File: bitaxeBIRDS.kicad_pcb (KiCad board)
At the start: 6 copper layers, 65 x 112 mm, 203 parts, among them J1001 XT30, J3001 Conn_01x04, J5001 Conn_01x04, J6 USB_C_Receptacle_USB2.0, SW1 SWITCH-SPST, SW2 SWITCH-SPST, U2001 TPSM861253RDXR, U2003 TPS546D24S, U2004 TPS546D24S, U27 RP2040, U3 TPS22919DCKR, U4001 MCP1824T-1202E/OT, U4002 25MHz, U4003 BM1370_mode1, U4004 MCP1824T-0802E, U4005 SN74AVC4T774, U4006 BM1370_mode1, U5001 EMC2103-2, U8 W25Q16JVUXIQ TR, U9 SK6812, Y1 12MHz

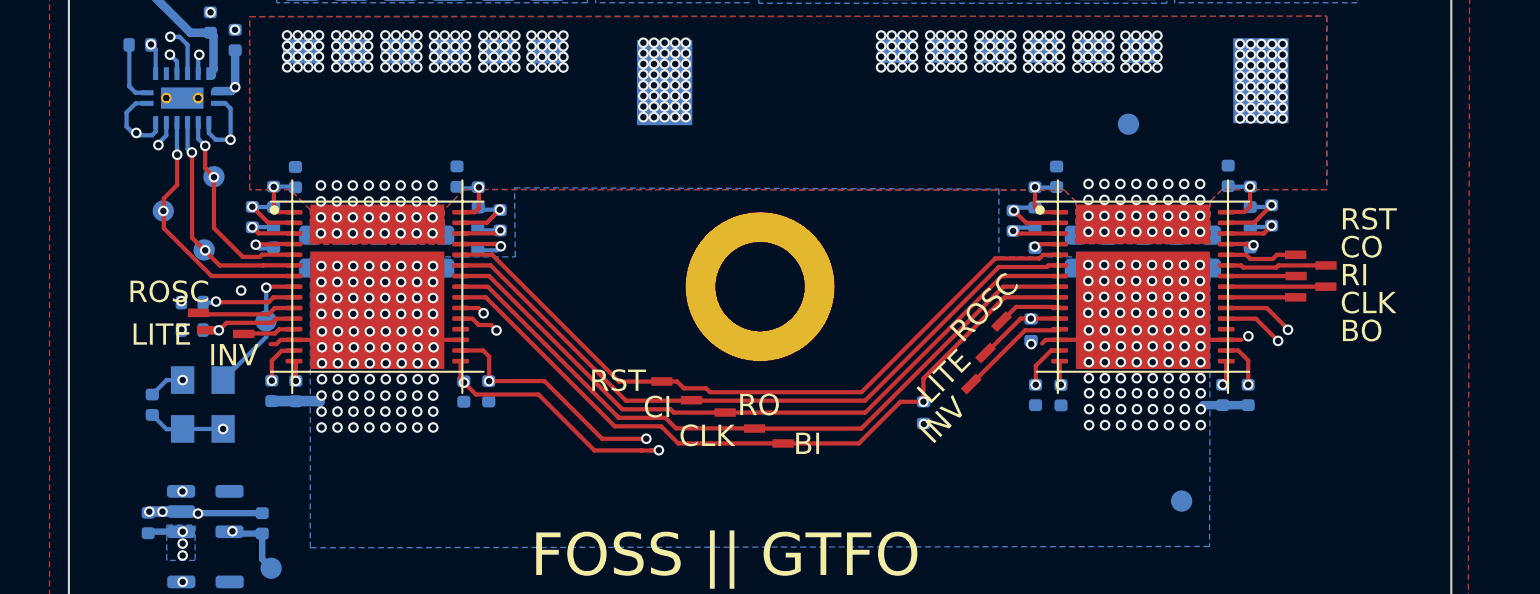
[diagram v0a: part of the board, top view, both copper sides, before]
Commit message: started to piece in the BZM2 into schematic
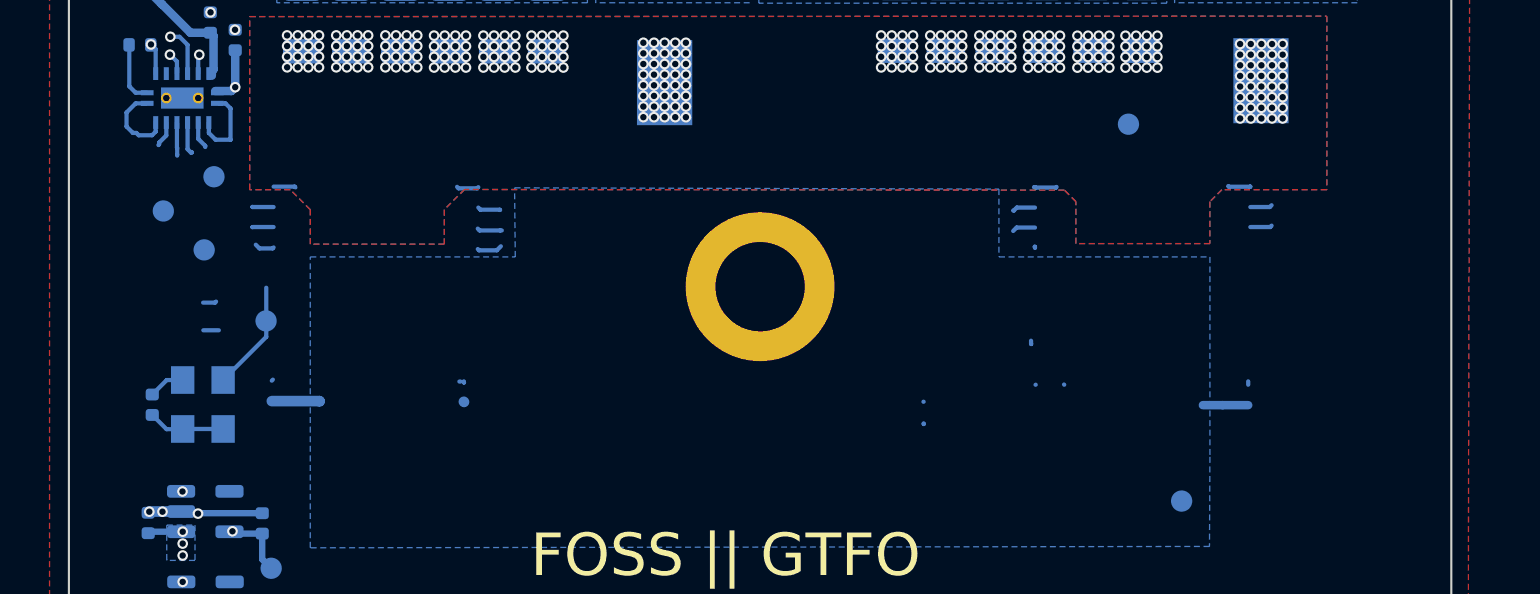
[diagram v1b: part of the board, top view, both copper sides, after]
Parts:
- removed C4002, C4003, C4004, C4005, C4006, C4008, C4012, C4013, C4015, C4016, C4018, C4020, C4023, C4025, C4026, C4027, C4028, C4029, C4031, C4033, C4034, C4036, C4038, C4040: 1uF, Capacitor_SMD:C_0402_1005Metric
- removed C4010, C4014, C4017, C4019, C4022, C4030, C4032, C4035, C4039, C4041: 10uF, Capacitor_SMD:C_0603_1608Metric
- removed R4001: 10k, Resistor_SMD:R_0402_1005Metric
- removed R4002, R4004: 1k, Resistor_SMD:R_0402_1005Metric
- removed R4003: 2k, Resistor_SMD:R_0402_1005Metric
- removed TP4001, TP4007: ROSC, bitaxe:TestPoint_Pad_1.0x0.4mm
- removed TP4002, TP4008: LITE, bitaxe:TestPoint_Pad_1.0x0.4mm
- removed TP4003, TP4017: INV, bitaxe:TestPoint_Pad_1.0x0.4mm
- removed TP4009, TP4021: RST, bitaxe:TestPoint_Pad_1.0x0.4mm
- removed TP4010: CI, bitaxe:TestPoint_Pad_1.0x0.4mm
- removed TP4011: RO, bitaxe:TestPoint_Pad_1.0x0.4mm
- removed TP4012, TP4024: CLK, bitaxe:TestPoint_Pad_1.0x0.4mm
- removed TP4013: BI, bitaxe:TestPoint_Pad_1.0x0.4mm
- removed TP4022: CO, bitaxe:TestPoint_Pad_1.0x0.4mm
- removed TP4023: RI, bitaxe:TestPoint_Pad_1.0x0.4mm
- removed TP4025: BO, bitaxe:TestPoint_Pad_1.0x0.4mm
- removed U4003, U4006: BM1370_mode1, bitaxe:BM1370
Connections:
- C103 pad 2: /Data/3V3 -> /3V3
- C104 pad 2: /Data/3V3 -> /3V3
- C105 pad 2: /Data/3V3 -> /3V3
- C106 pad 2: /Data/3V3 -> /3V3
- C107 pad 2: /Data/3V3 -> /3V3
- C108 pad 2: /Data/3V3 -> /3V3
- C109 pad 2: /Data/3V3 -> /3V3
- C110 pad 2: /Data/3V3 -> /3V3
- C4001 pad 1: GND -> /ASIC/GND
- C4007 pad 1: GND -> /ASIC/GND
- C4009 pad 2: GND -> /ASIC/GND
- C4011 pad 1: GND -> /ASIC/GND
- C4021 pad 1: GND -> /ASIC/GND
- C4024 pad 2: GND -> /ASIC/GND
- C4037 pad 2: GND -> /ASIC/GND
- C99 pad 2: /Data/3V3 -> /3V3
- J3001 pad 2: /Data/3V3 -> /3V3
- R1 pad 2: /Data/3V3 -> /3V3
- R19 pad 1: /Data/3V3 -> /3V3
- R20 pad 2: /Data/3V3 -> /3V3
- R34 pad 2: /Data/3V3 -> /3V3
- R4005 pad 1: GND -> /ASIC/GND
- R50 pad 1: /Data/3V3 -> /3V3
- R5001 pad 2: /ASIC/TEMP2_P -> /fan/TEMP2_P
- R5002 pad 2: /ASIC/TEMP2_N -> /fan/TEMP2_N
- R5003 pad 2: /ASIC/TEMP1_P -> /fan/TEMP1_P
- R5004 pad 2: /ASIC/TEMP1_N -> /fan/TEMP1_N
- U27 pad 1: /Data/3V3 -> /3V3
- U27 pad 10: /Data/3V3 -> /3V3
- U27 pad 22: /Data/3V3 -> /3V3
- U27 pad 33: /Data/3V3 -> /3V3
- U27 pad 42: /Data/3V3 -> /3V3
- U27 pad 43: /Data/3V3 -> /3V3
- U27 pad 44: /Data/3V3 -> /3V3
- U27 pad 48: /Data/3V3 -> /3V3
- U27 pad 49: /Data/3V3 -> /3V3
- U4001 pad 2: GND -> /ASIC/GND
- U4002 pad 2: GND -> /ASIC/GND
- U4004 pad 2: GND -> /ASIC/GND
- U4005 pad 1: GND -> /ASIC/GND
- U4005 pad 10: GND -> /ASIC/GND
- U4005 pad 2: GND -> /ASIC/GND
- U4005 pad 6: GND -> /ASIC/GND
- U8 pad 8: /Data/3V3 -> /3V3
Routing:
- net /ASIC/TEMP2_N: track 54.9 -> 0.00 mm, vias 2 -> 0
- net /ASIC/TEMP2_P: track 51.9 -> 0.00 mm, vias 2 -> 0
- net Net-(U4003-VDD3_1): track 40.5 -> 0.00 mm, vias 2 -> 0
- net Net-(U4003-VDD2_1): track 38.5 -> 0.00 mm, vias 2 -> 0
- net Net-(U4003-VDD1_1): track 37.8 -> 0.00 mm, vias 2 -> 0
- net /fan/TEMP2_N: track 0.00 -> 37.5 mm, vias 0 -> 1
- net GND: track 94.4 -> 57.3 mm, vias 574 -> 376
- net /fan/TEMP2_P: track 0.00 -> 35.7 mm, vias 0 -> 1
- net Net-(U4003-BO): track 34.5 -> 0.00 mm, vias 1 -> 0
- net Net-(U4003-CLKO): track 33.8 -> 0.00 mm
- net /ASIC/1V2: track 103.9 -> 70.3 mm, vias 7 -> 2
- net Net-(U4003-NRSTO): track 33.5 -> 0.00 mm
- net Net-(U4003-RI): track 33.5 -> 0.00 mm
- net Net-(U4003-CO): track 33.4 -> 0.00 mm
- net /ASIC/0V8: track 57.4 -> 24.2 mm, vias 4 -> 1
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
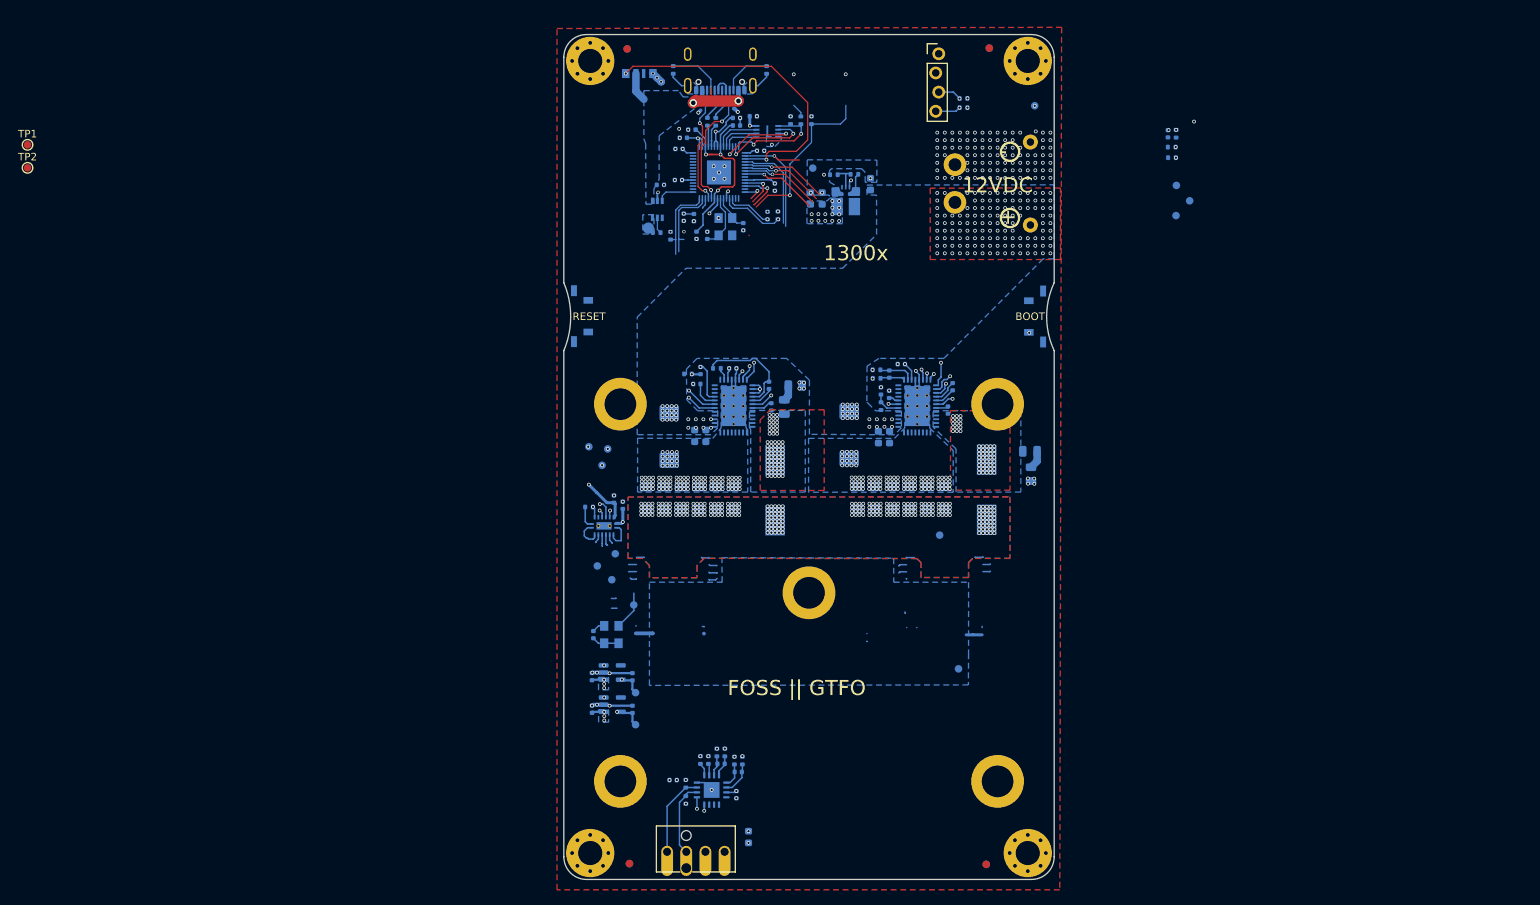
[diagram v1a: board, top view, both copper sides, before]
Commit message: finished adding ASICs to schematic. Change VR to single phase 2.8V output
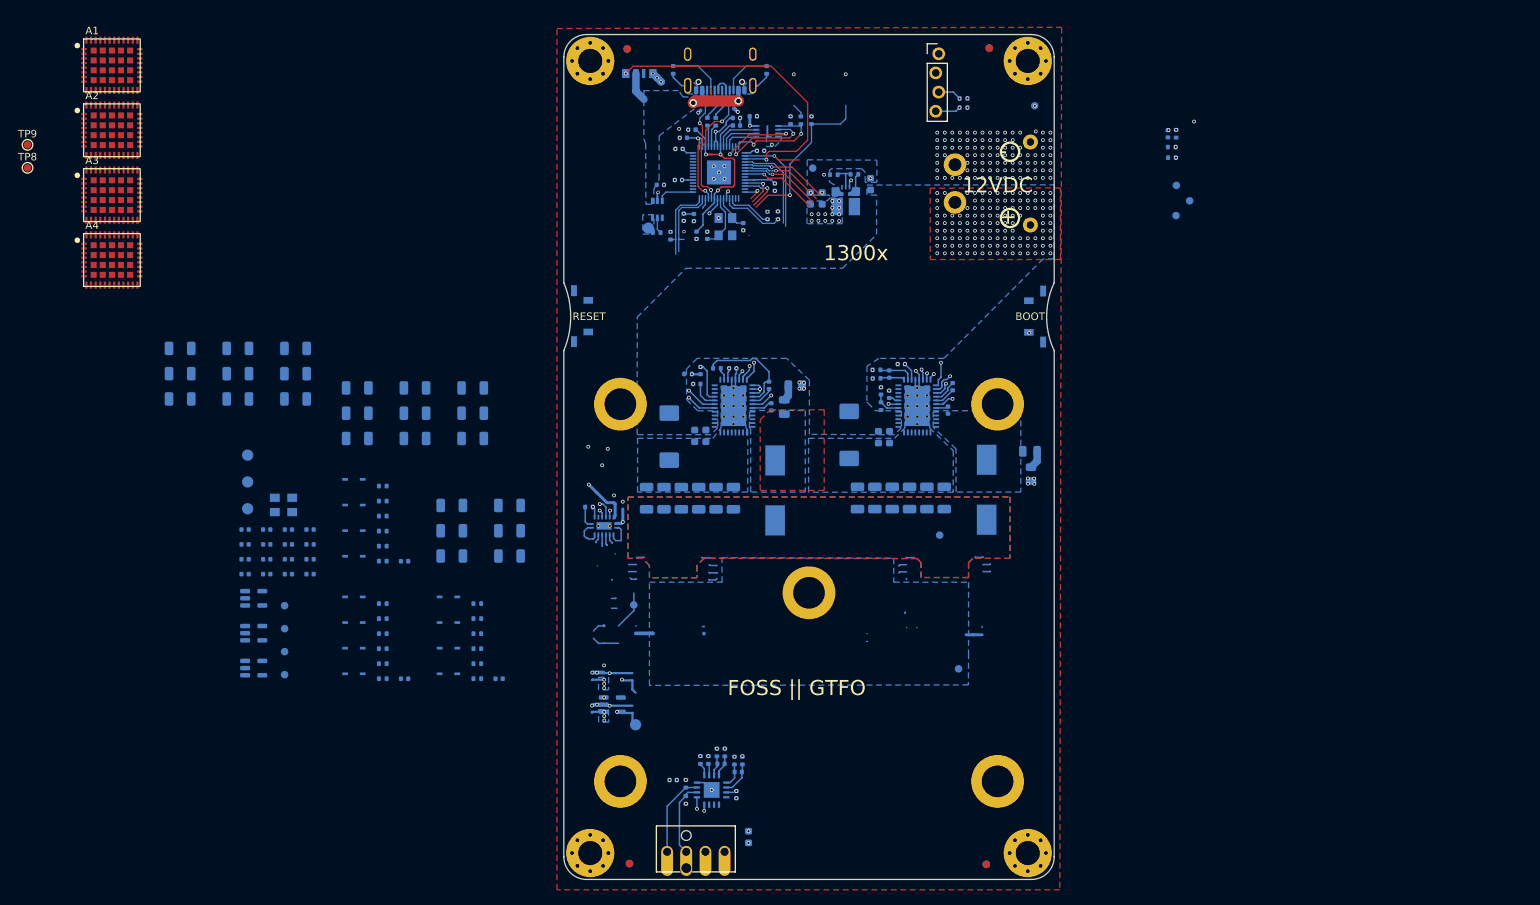
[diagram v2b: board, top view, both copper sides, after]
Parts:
- removed C4001, C4007, C4011, C4021: 1uF, Capacitor_SMD:C_0402_1005Metric
- removed C4009, C4024, C4037: 0.1uF, Capacitor_SMD:C_0402_1005Metric
- removed TP4006: 0V8, bitaxe:TestPoint_Pad_D1.0mm
- removed TP4014, TP4018: RST, bitaxe:TestPoint_Pad_D1.0mm
- removed TP4015, TP4019: TX, bitaxe:TestPoint_Pad_D1.0mm
- removed TP4016, TP4020: RX, bitaxe:TestPoint_Pad_D1.0mm
- removed U4002: 25MHz, bitaxe:SMD3225-4P
- removed U4004: MCP1824T-0802E, Package_TO_SOT_SMD:SOT-23-5
- added A1: BZM2_MODE0, bitaxe:bzm2, F.Cu at (38.6, 42.1)
- added A2: BZM2_MODE1, bitaxe:bzm2, F.Cu at (38.6, 50.7)
- added A3: BZM2_MODE0, bitaxe:bzm2, F.Cu at (38.6, 59.3)
- added A4: BZM2_MODE1, bitaxe:bzm2, F.Cu at (38.6, 67.9)
- added C100: 100uF, Capacitor_SMD:C_1206_3216Metric, B.Cu at (86.4, 88.2)
- added C101: 100uF, Capacitor_SMD:C_1206_3216Metric, B.Cu at (86.4, 84.8)
- added C107: 100uF, Capacitor_SMD:C_1206_3216Metric, B.Cu at (78.8, 91.5)
- added C108: 100uF, Capacitor_SMD:C_1206_3216Metric, B.Cu at (78.8, 88.2)
- added C109: 100uF, Capacitor_SMD:C_1206_3216Metric, B.Cu at (78.8, 84.8)
- added C115: 100uF, Capacitor_SMD:C_1206_3216Metric, B.Cu at (55.3, 86.3)
- added C116: 100uF, Capacitor_SMD:C_1206_3216Metric, B.Cu at (55.3, 83.0)
- added C117: 100uF, Capacitor_SMD:C_1206_3216Metric, B.Cu at (55.3, 79.6)
- added C123: 100uF, Capacitor_SMD:C_1206_3216Metric, B.Cu at (62.9, 86.3)
- added C124: 100uF, Capacitor_SMD:C_1206_3216Metric, B.Cu at (62.9, 83.0)
- added C125: 100uF, Capacitor_SMD:C_1206_3216Metric, B.Cu at (62.9, 79.6)
- added C131: 100uF, Capacitor_SMD:C_1206_3216Metric, B.Cu at (47.6, 86.3)
- added C132: 100uF, Capacitor_SMD:C_1206_3216Metric, B.Cu at (47.6, 83.0)
- added C133: 100uF, Capacitor_SMD:C_1206_3216Metric, B.Cu at (47.6, 79.6)
- added C139: 100uF, Capacitor_SMD:C_1206_3216Metric, B.Cu at (71.1, 91.5)
- added C140: 100uF, Capacitor_SMD:C_1206_3216Metric, B.Cu at (71.1, 88.2)
- added C141: 100uF, Capacitor_SMD:C_1206_3216Metric, B.Cu at (71.1, 84.8)
- added C142: 1000pF, Capacitor_SMD:C_0402_1005Metric, B.Cu at (77.4, 123.4)
- added C143: 1000pF, Capacitor_SMD:C_0402_1005Metric, B.Cu at (77.4, 107.8)
- added C144: 1000pF, Capacitor_SMD:C_0402_1005Metric, B.Cu at (89.9, 123.4)
- added C57: 0.1uF, Capacitor_SMD:C_0402_1005Metric, B.Cu at (56.2, 109.5)
- added C58: 0.1uF, Capacitor_SMD:C_0402_1005Metric, B.Cu at (56.2, 107.6)
- added C59: 0.1uF, Capacitor_SMD:C_0402_1005Metric, B.Cu at (56.2, 105.6)
- added C60: 120pF, Capacitor_SMD:C_0402_1005Metric, B.Cu at (56.2, 103.6)
- added C61: 120pF, Capacitor_SMD:C_0402_1005Metric, B.Cu at (59.1, 109.5)
- added C62: 120pF, Capacitor_SMD:C_0402_1005Metric, B.Cu at (59.1, 107.6)
- added C63: 120pF, Capacitor_SMD:C_0402_1005Metric, B.Cu at (59.1, 105.6)
- added C64: 120pF, Capacitor_SMD:C_0402_1005Metric, B.Cu at (59.1, 103.6)
- added C65: 1uF, Capacitor_SMD:C_0402_1005Metric, B.Cu at (62.0, 109.5)
- added C66: 1uF, Capacitor_SMD:C_0402_1005Metric, B.Cu at (62.0, 107.6)
- added C67: 1uF, Capacitor_SMD:C_0402_1005Metric, B.Cu at (62.0, 105.6)
- added C68: 1uF, Capacitor_SMD:C_0402_1005Metric, B.Cu at (62.0, 103.6)
- added C69: 1uF, Capacitor_SMD:C_0402_1005Metric, B.Cu at (64.9, 109.5)
- added C70: 1uF, Capacitor_SMD:C_0402_1005Metric, B.Cu at (64.9, 107.6)
- added C71: 1uF, Capacitor_SMD:C_0402_1005Metric, B.Cu at (64.9, 105.6)
- added C72: 1uF, Capacitor_SMD:C_0402_1005Metric, B.Cu at (64.9, 103.6)
- added C83: 100uF, Capacitor_SMD:C_1206_3216Metric, B.Cu at (91.3, 107.1)
- added C84: 100uF, Capacitor_SMD:C_1206_3216Metric, B.Cu at (91.3, 103.8)
- added C85: 100uF, Capacitor_SMD:C_1206_3216Metric, B.Cu at (91.3, 100.4)
- added C91: 100uF, Capacitor_SMD:C_1206_3216Metric, B.Cu at (83.7, 107.1)
- added C92: 100uF, Capacitor_SMD:C_1206_3216Metric, B.Cu at (83.7, 103.8)
- added C93: 100uF, Capacitor_SMD:C_1206_3216Metric, B.Cu at (83.7, 100.4)
- added C99: 100uF, Capacitor_SMD:C_1206_3216Metric, B.Cu at (86.4, 91.5)
- added D1: 1SS380VMTE-17, bitaxe:SOD-323FLUMD2_ROM, B.Cu at (70.7, 122.7)
- added D10: 1SS380VMTE-17, bitaxe:SOD-323FLUMD2_ROM, B.Cu at (83.2, 119.3)
- added D11: 1SS380VMTE-17, bitaxe:SOD-323FLUMD2_ROM, B.Cu at (83.2, 115.9)
- added D12: 1SS380VMTE-17, bitaxe:SOD-323FLUMD2_ROM, B.Cu at (83.2, 112.5)
- added D2: 1SS380VMTE-17, bitaxe:SOD-323FLUMD2_ROM, B.Cu at (70.7, 119.3)
- added D3: 1SS380VMTE-17, bitaxe:SOD-323FLUMD2_ROM, B.Cu at (70.7, 115.9)
- added D4: 1SS380VMTE-17, bitaxe:SOD-323FLUMD2_ROM, B.Cu at (70.7, 112.5)
- added D5: 1SS380VMTE-17, bitaxe:SOD-323FLUMD2_ROM, B.Cu at (70.7, 107.2)
- added D6: 1SS380VMTE-17, bitaxe:SOD-323FLUMD2_ROM, B.Cu at (70.7, 103.8)
- added D7: 1SS380VMTE-17, bitaxe:SOD-323FLUMD2_ROM, B.Cu at (70.7, 100.4)
- added D8: 1SS380VMTE-17, bitaxe:SOD-323FLUMD2_ROM, B.Cu at (70.7, 97.0)
- added D9: 1SS380VMTE-17, bitaxe:SOD-323FLUMD2_ROM, B.Cu at (83.2, 122.7)
- added R35: 1k, Resistor_SMD:R_0402_1005Metric, B.Cu at (74.5, 123.4)
- added R36: 1k, Resistor_SMD:R_0402_1005Metric, B.Cu at (74.5, 121.4)
- added R37: 1k, Resistor_SMD:R_0402_1005Metric, B.Cu at (74.5, 119.4)
- added R38: 1k, Resistor_SMD:R_0402_1005Metric, B.Cu at (74.5, 117.4)
- added R39: 1k, Resistor_SMD:R_0402_1005Metric, B.Cu at (74.5, 115.4)
- added R40: 1k, Resistor_SMD:R_0402_1005Metric, B.Cu at (74.5, 113.4)
- added R41: 1k, Resistor_SMD:R_0402_1005Metric, B.Cu at (74.5, 107.8)
- added R42: 1k, Resistor_SMD:R_0402_1005Metric, B.Cu at (74.5, 105.8)
- added R43: 1k, Resistor_SMD:R_0402_1005Metric, B.Cu at (74.5, 103.8)
- added R44: 1k, Resistor_SMD:R_0402_1005Metric, B.Cu at (74.5, 101.8)
- added R45: 1k, Resistor_SMD:R_0402_1005Metric, B.Cu at (74.5, 99.8)
- added R46: 1k, Resistor_SMD:R_0402_1005Metric, B.Cu at (74.5, 97.9)
- added R47: 1k, Resistor_SMD:R_0402_1005Metric, B.Cu at (87.0, 123.4)
- added R48: 1k, Resistor_SMD:R_0402_1005Metric, B.Cu at (87.0, 121.4)
- added R49: 1k, Resistor_SMD:R_0402_1005Metric, B.Cu at (87.0, 119.4)
- added R50: 1k, Resistor_SMD:R_0402_1005Metric, B.Cu at (87.0, 117.4)
- added R51: 1k, Resistor_SMD:R_0402_1005Metric, B.Cu at (87.0, 115.4)
- added R52: 1k, Resistor_SMD:R_0402_1005Metric, B.Cu at (87.0, 113.4)
- added TP11: CLKI, TestPoint:TestPoint_Pad_D1.0mm, B.Cu at (61.5, 122.9)
- added TP12: CLKI, TestPoint:TestPoint_Pad_D1.0mm, B.Cu at (61.5, 119.8)
- added TP13: CLKI, TestPoint:TestPoint_Pad_D1.0mm, B.Cu at (61.5, 116.8)
- added TP14: CLKI, TestPoint:TestPoint_Pad_D1.0mm, B.Cu at (61.5, 113.7)
- added TP15: 1V2-4, TestPoint:TestPoint_Pad_D1.5mm, B.Cu at (56.6, 100.9)
- added TP16: 1V2-3, TestPoint:TestPoint_Pad_D1.5mm, B.Cu at (56.6, 97.3)
- added TP17: 1V2-2, TestPoint:TestPoint_Pad_D1.5mm, B.Cu at (56.6, 93.8)
- added U10: MCP1824T-1202E/OT, Package_TO_SOT_SMD:SOT-23-5, B.Cu at (57.4, 117.4)
- added U11: MCP1824T-1202E/OT, Package_TO_SOT_SMD:SOT-23-5, B.Cu at (57.4, 112.7)
- added U9: MCP1824T-1202E/OT, Package_TO_SOT_SMD:SOT-23-5, B.Cu at (57.4, 122.0)
- added Y2: 50MHz, bitaxe:OSC_ECS-3225MV-500-CN-TR, B.Cu at (61.3, 100.4)
- TP10: renamed from TP4005; footprint bitaxe:TestPoint_Pad_D1.0mm -> TestPoint:TestPoint_Pad_D1.0mm
- TP18: renamed from TP4004; value 1V2 -> 1V2-1; footprint bitaxe:TestPoint_Pad_D1.0mm -> TestPoint:TestPoint_Pad_D1.5mm
- renumbered C2001 to C1, C2012 to C10, C2013 to C11, C2016 to C14, C2017 to C15, C2018 to C16, C2004 to C2, C2023 to C21, C2024 to C22, C2025 to C23, C2026 to C24, C2027 to C25, C2028 to C26, C2029 to C27, C2030 to C28, C2031 to C29, C2005 to C3, C2032 to C30, C2033 to C31, C2034 to C32, C2035 to C33, C2036 to C34, C2037 to C35, C2038 to C36, C2039 to C37, C2040 to C38, C2041 to C39, C2006 to C4, C2042 to C40, C2043 to C41, C96 to C42, C97 to C43, C99 to C44, C26 to C45, C100 to C46, C101 to C47, C102 to C48, C103 to C49, C2007 to C5, C104 to C50, C105 to C51, C106 to C52, C107 to C53, C108 to C54, C109 to C55, C110 to C56, C2008 to C6, C2009 to C7, C5001 to C73, C5002 to C74, C5003 to C75, C5004 to C76, C5005 to C77, C2010 to C8, C2011 to C9, FID1001 to FID1, FID1002 to FID2, FID1003 to FID3, FID1004 to FID4, H1001 to H1, H1002 to H2, H1003 to H3, H1004 to H4, HS1001 to HS1, J1001 to J1, J6 to J2, J3001 to J3, J5001 to J4, L2001 to L1, L2002 to L2, NT2001 to NT1, NT2002 to NT2, R2001 to R1, R2010 to R10, R2011 to R11, R2012 to R12, R2013 to R13, R2014 to R14, R50 to R15, R51 to R16, R52 to R17, R55 to R18, R34 to R19, R2002 to R2, R2 to R20, R53 to R21, R54 to R22, R19 to R23, R20 to R24, R1 to R25, R4005 to R26, R5001 to R27, R5002 to R28, R5003 to R29, R2003 to R3, R5004 to R30, R5005 to R31, R5006 to R32, R5007 to R33, R5008 to R34, R2004 to R4, R2005 to R5, R2006 to R6, R2007 to R7, R2008 to R8, R2009 to R9, TP2002 to TP1, TP2003 to TP2, TP2004 to TP3, TP2005 to TP4, TP2006 to TP5, TP2007 to TP6, TP2008 to TP7, TP2 to TP8, TP1 to TP9, U2001 to U1, U4001 to U12, U5001 to U13, U2003 to U2, U2004 to U3, U8 to U4, U3 to U5, U27 to U6, U9 to U7, U4005 to U8
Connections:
- R20 pad 1: /Data/5V_SWITCH -> /5V_SWITCH
- R26 pad 1: /ASIC/GND -> GND
- TP10 pad 1: /ASIC/CLKI -> /ASIC/REFCLKIN1
- TP18 pad 1: /ASIC/1V2 -> /ASIC/1V2-1
- U12 pad 1: /5V -> /5V_SWITCH
- U12 pad 2: /ASIC/GND -> GND
- U12 pad 3: /5V -> /5V_SWITCH
- U12 pad 5: /ASIC/1V2 -> /ASIC/1V2-1
- U5 pad 6: /Data/5V_SWITCH -> /5V_SWITCH
- U6 pad 11: /Data/TXD -> /ASIC/RX_3V3
- U6 pad 12: /Data/RXD -> /ASIC/TX_3V3
- U6 pad 13: unconnected-(U27-GPIO10-Pad13) -> /ASIC/TRIP_3V3
- U6 pad 14: /Data/RST -> /ASIC/RST_3V3
- U6 pad 4: /Data/THERM -> unconnected-(U6-GPIO2-Pad4)
- U8 pad 1: /ASIC/GND -> GND
- U8 pad 10: /ASIC/GND -> GND
- U8 pad 11: unconnected-(U4005-B4-Pad11) -> /ASIC/TRIP_3V3
- U8 pad 16: /ASIC/1V2 -> /ASIC/1V2-1
- U8 pad 2: /ASIC/GND -> /ASIC/1V2-1
- U8 pad 6: /ASIC/GND -> /ASIC/TRIP_1V2
- U8 pad 7: /ASIC/1V2 -> GND
- U8 pad 8: /ASIC/1V2 -> /ASIC/1V2-1
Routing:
- net /ASIC/1V2: track 70.3 -> 3.74 mm, vias 2 -> 0
- net /ASIC/1V2-1: track 0.00 -> 62.7 mm, vias 0 -> 2
- net (no net): track 14.3 -> 45.7 mm, vias 0 -> 6
- net GND: track 57.3 -> 83.0 mm, vias 376 -> 157
- net /ASIC/0V8: track 24.2 -> 0.00 mm, vias 1 -> 0
- net /ASIC/GND: track 19.2 -> 0.00 mm, vias 9 -> 0
- net unconnected-(U6-GPIO2-Pad4): track 0.00 -> 12.4 mm
- net /Data/THERM: track 12.4 -> 0.00 mm
- net unconnected-(U6-GPIO4-Pad6): track 11.2 -> 0.00 mm, vias 1 -> 0
- net /Data/RXD: track 6.04 -> 0.00 mm, vias 1 -> 0
- net /ASIC/TX_3V3: track 21.6 -> 27.7 mm, vias 2 -> 3
- net /Data/TXD: track 5.39 -> 0.00 mm, vias 1 -> 0
- net /ASIC/RX_3V3: track 20.9 -> 26.3 mm, vias 2 -> 3
- net /ASIC/REFCLKIN1: track 0.00 -> 5.18 mm
- net /ASIC/CLKI: track 5.18 -> 0.00 mm
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- added copper zone on B.Cu, net /5V_SWITCH
- removed copper zone on B.Cu, net /Data/5V_SWITCH
- removed copper zone on F.Cu, net /Power/SW1
